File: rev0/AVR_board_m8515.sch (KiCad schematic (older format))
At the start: 10 parts

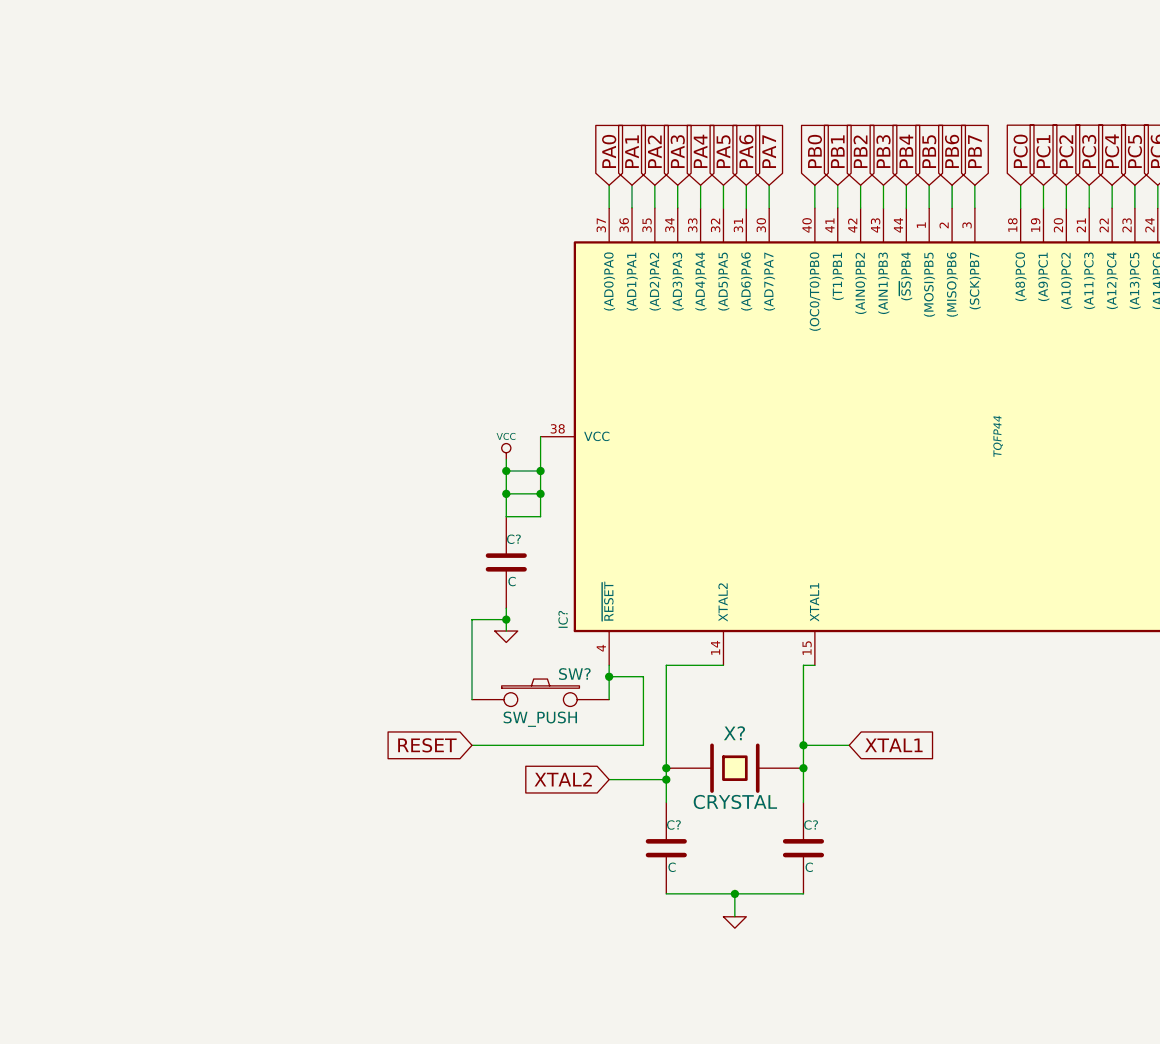
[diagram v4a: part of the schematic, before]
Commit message: added smd crystal to schematic and an LED on PE1
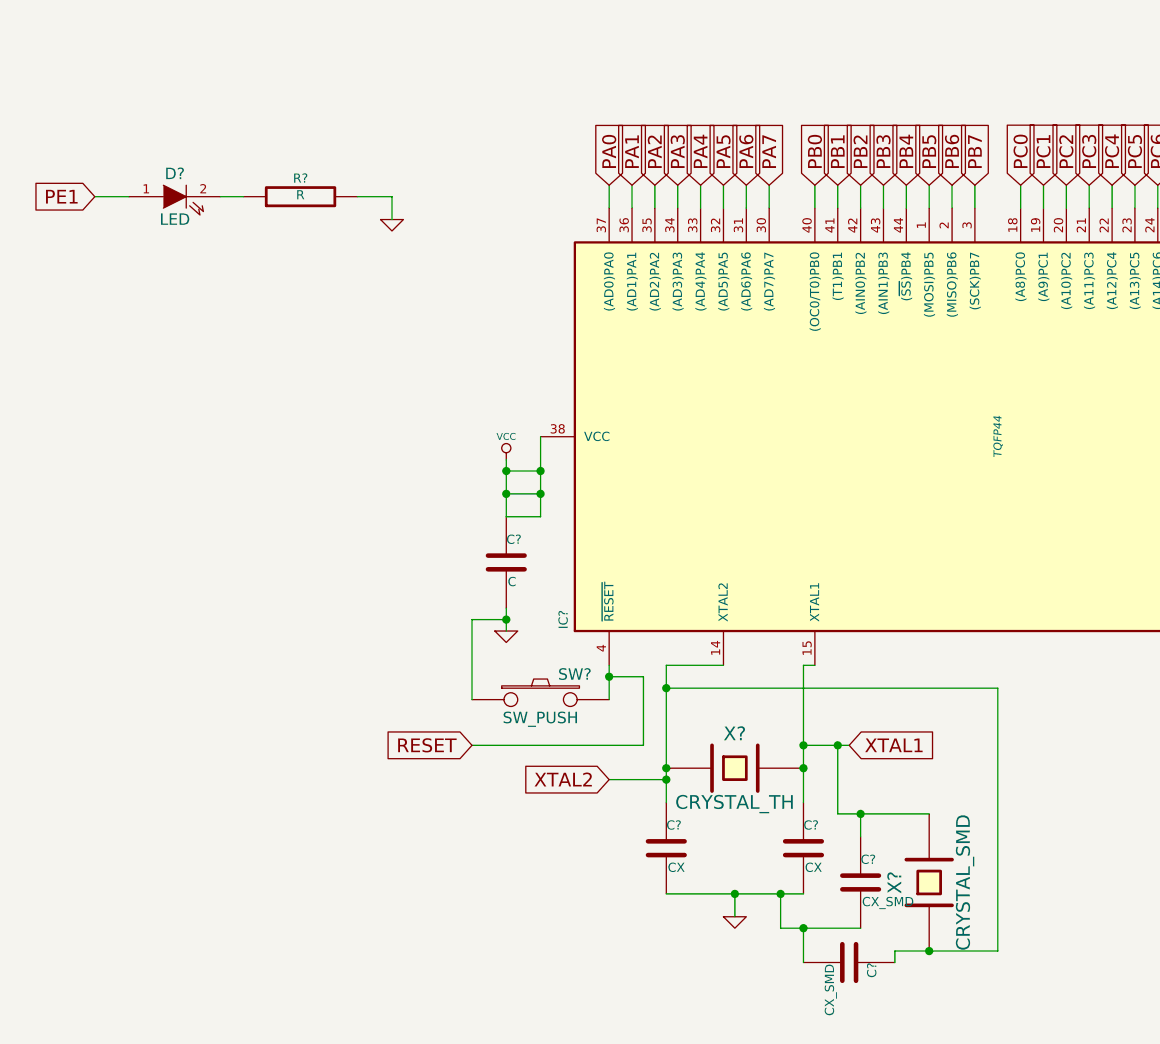
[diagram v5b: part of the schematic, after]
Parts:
- added C? (x2): CX_SMD, symbol C
- added D?: LED, symbol LED
- added R?: R, symbol R
- added X?: CRYSTAL_SMD, symbol CRYSTAL
- C? (x2): value C -> CX
- X?: value CRYSTAL -> CRYSTAL_TH
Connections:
- net GND: now also C?.2, C?.2, R?.2
- net PE1: now also D?.1 (A)
- net XTAL1: now also C?.1, X?.2
- net XTAL2: now also C?.1, X?.1
- new net: D?.2 (K), R?.1
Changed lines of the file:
@@
 P 4500 6400
 F 0 "X?" H 4500 6550 60  0000 C CNN
-F 1 "CRYSTAL" H 4500 6250 60  0000 C CNN
+F 1 "CRYSTAL_TH" H 4500 6250 60  0000 C CNN
 F 2 "" H 4500 6400 60  0000 C CNN
 F 3 "" H 4500 6400 60  0000 C CNN
@@
 P 4800 6750
 F 0 "C?" H 4800 6850 40  0000 L CNN
-F 1 "C" H 4806 6665 40  0000 L CNN
+F 1 "CX" H 4806 6665 40  0000 L CNN
 F 2 "" H 4838 6600 30  0000 C CNN
 F 3 "" H 4800 6750 60  0000 C CNN
@@
 P 4200 6750
 F 0 "C?" H 4200 6850 40  0000 L CNN
-F 1 "C" H 4206 6665 40  0000 L CNN
+F 1 "CX" H 4206 6665 40  0000 L CNN
 F 2 "" H 4238 6600 30  0000 C CNN
 F 3 "" H 4200 6750 60  0000 C CNN
@@
 XTAL2
 Wire Wire Line
-	5000 6300 4800 6300
+	4800 6300 5000 6300
 Connection ~ 4800 6300
 Wire Wire Line
@@
 Connection ~ 3650 5200
 Wire Wire Line
-	3950 6100 3950 5950
+	3950 5950 3950 6100
 Wire Wire Line
 	4100 6000 3950 6000
@@
 Wire Wire Line
 	4750 1850 4600 1850
+$Comp
+L CRYSTAL X?
+U 1 1 5418E675
+P 5350 6900
+F 0 "X?" H 5350 7050 60  0000 C CNN
+F 1 "CRYSTAL_SMD" H 5350 6750 60  0000 C CNN
+F 2 "" H 5350 6900 60  0000 C CNN
+F 3 "" H 5350 6900 60  0000 C CNN
+	1    5350 6900
+	0    -1   -1   0
+$EndComp
+Wire Wire Line
+	5350 6600 4950 6600
+Wire Wire Line
+	4950 6600 4950 6300
+Connection ~ 4950 6300
+Wire Wire Line
+	5200 7200 5650 7200
+Wire Wire Line
+	5650 7200 5650 6050
+Wire Wire Line
+	5650 6050 4200 6050
+Connection ~ 4200 6050
+$Comp
+L C C?
+U 1 1 5418E983
+P 5050 6900
+F 0 "C?" H 5050 7000 40  0000 L CNN
+F 1 "CX_SMD" H 5056 6815 40  0000 L CNN
+F 2 "" H 5088 6750 30  0000 C CNN
+F 3 "" H 5050 6900 60  0000 C CNN
+	1    5050 6900
+	1    0    0    -1
+$EndComp
+Wire Wire Line
+	5050 6700 5050 6600
+Connection ~ 5050 6600
+Wire Wire Line
+	5050 7100 4700 7100
+Wire Wire Line
+	4700 7100 4700 6950
+Connection ~ 4700 6950
+$Comp
+L C C?
+U 1 1 5418EAF3
+P 5000 7250
+F 0 "C?" H 5000 7350 40  0000 L CNN
+F 1 "CX_SMD" H 5006 7165 40  0000 L CNN
+F 2 "" H 5038 7100 30  0000 C CNN
+F 3 "" H 5000 7250 60  0000 C CNN
+	1    5000 7250
+	0    1    1    0
+$EndComp
+Wire Wire Line
+	5200 7200 5200 7250
+Connection ~ 5350 7200
+Wire Wire Line
+	4800 7250 4800 7100
+Connection ~ 4800 7100
+$Comp
+L LED D?
+U 1 1 5418EEE7
+P 2050 3900
+F 0 "D?" H 2050 4000 50  0000 C CNN
+F 1 "LED" H 2050 3800 50  0000 C CNN
+F 2 "" H 2050 3900 60  0000 C CNN
+F 3 "" H 2050 3900 60  0000 C CNN
+	1    2050 3900
+	1    0    0    -1
+$EndComp
+Text GLabel 1700 3900 0    60   Input ~ 0
+PE1
+$Comp
+L R R?
+U 1 1 5418EEF6
+P 2600 3900
+F 0 "R?" V 2680 3900 40  0000 C CNN
+F 1 "R" V 2607 3901 40  0000 C CNN
+F 2 "" V 2530 3900 30  0000 C CNN
+F 3 "" H 2600 3900 30  0000 C CNN
+	1    2600 3900
+	0    -1   -1   0
+$EndComp
+Wire Wire Line
+	1700 3900 1850 3900
+Wire Wire Line
+	2250 3900 2350 3900
+$Comp
+L GND #PWR?
+U 1 1 5418F076
+P 3000 4000
+F 0 "#PWR?" H 3000 4000 30  0001 C CNN
+F 1 "GND" H 3000 3930 30  0001 C CNN
+F 2 "" H 3000 4000 60  0000 C CNN
+F 3 "" H 3000 4000 60  0000 C CNN
+	1    3000 4000
+	1    0    0    -1
+$EndComp
+Wire Wire Line
+	2850 3900 3000 3900
+Wire Wire Line
+	3000 3900 3000 4000
 $EndSCHEMATC
